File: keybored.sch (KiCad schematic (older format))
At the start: 24 parts, among them SW1 SW_Push, U1 ATmega32U4-AU, Y1 16MHz

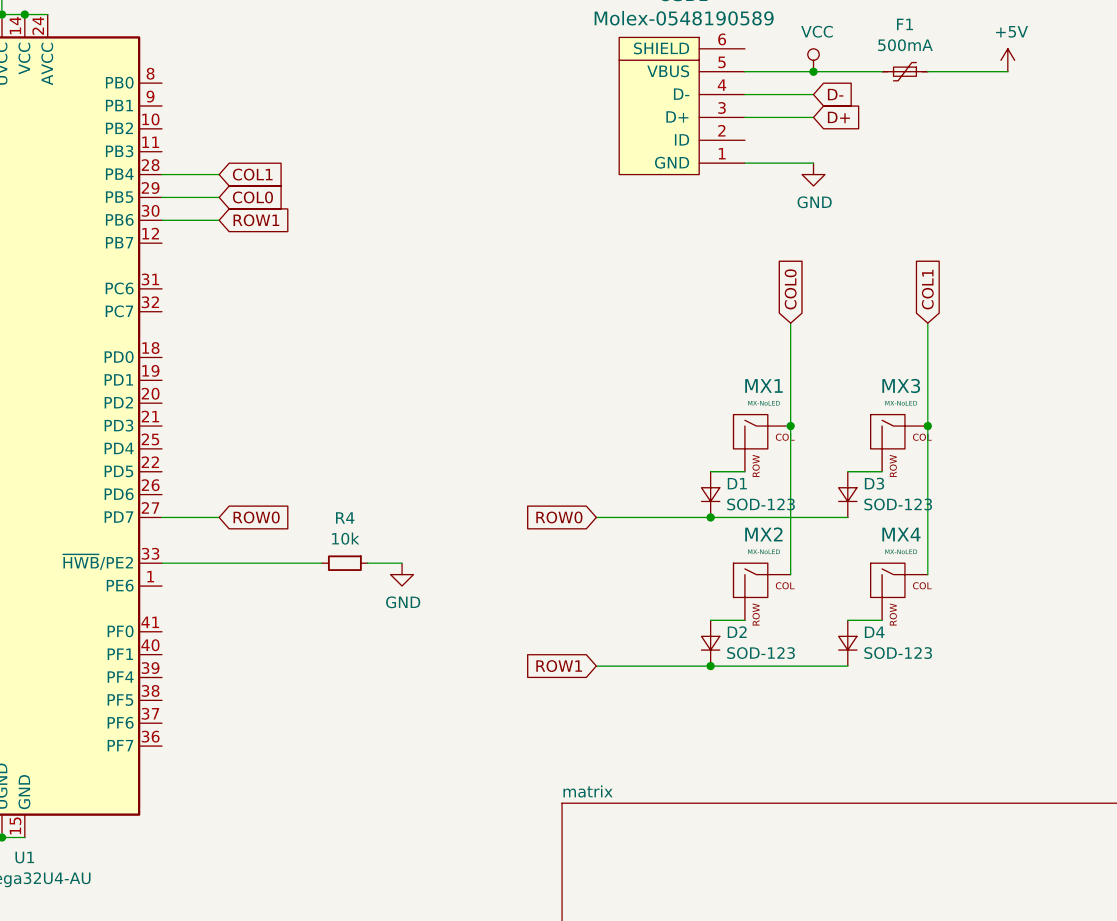
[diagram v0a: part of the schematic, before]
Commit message: updated main board schematic
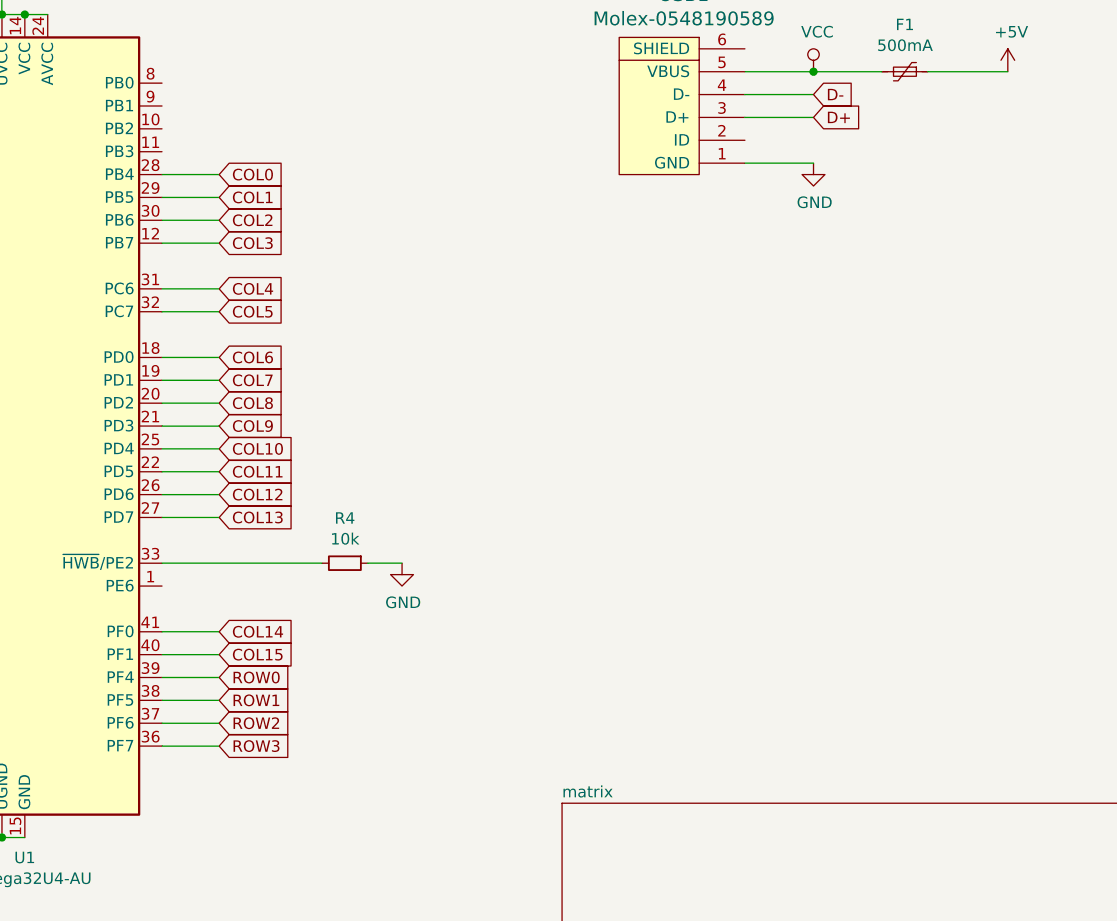
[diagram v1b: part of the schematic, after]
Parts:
- removed D1, D2, D3, D4: SOD-123, Diode_SMD:D_SOD-123, symbol Device:D_Small
- removed MX1, MX2, MX3, MX4: MX-NoLED, MX_Alps_Hybrid:MX-1U, symbol MX_Alps_Hybrid:MX-NoLED
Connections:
- net COL0: now also U1.28 (PB4); no longer U1.29 (PB5)
- net COL1: now also U1.29 (PB5); no longer U1.28 (PB4)
- net ROW0: now also U1.39 (PF4); no longer U1.27 (PD7)
- net ROW1: now also U1.38 (PF5); no longer U1.30 (PB6)
- net COL3: now reaches U1.12 (PB7)
- net COL6: now reaches U1.18 (PD0)
- net COL7: now reaches U1.19 (PD1)
- net COL8: now reaches U1.20 (PD2)
- net COL9: now reaches U1.21 (PD3)
- net COL11: now reaches U1.22 (PD5)
- net COL10: now reaches U1.25 (PD4)
- net COL12: now reaches U1.26 (PD6)
- net COL4: now reaches U1.31 (PC6)
- net COL5: now reaches U1.32 (PC7)
- net ROW3: now reaches U1.36 (PF7)
- net ROW2: now reaches U1.37 (PF6)
- net COL15: now reaches U1.40 (PF1)
- net COL14: now reaches U1.41 (PF0)
- new net COL13: U1.27 (PD7)
- new net COL2: U1.30 (PB6)
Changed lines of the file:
@@
 $Descr A4 11693 8268
 encoding utf-8
-Sheet 1 1
+Sheet 1 2
 Title ""
 Date ""
@@
 Wire Wire Line
 	7150 2150 6850 2150
-$Comp
-L MX_Alps_Hybrid:MX-NoLED MX1
-U 1 1 5F5BD9E0
-P 6900 3350
-F 0 "MX1" H 6933 3573 60  0000 C CNN
-F 1 "MX-NoLED" H 6933 3499 20  0000 C CNN
-F 2 "MX_Alps_Hybrid:MX-1U" H 6275 3325 60  0001 C CNN
-F 3 "" H 6275 3325 60  0001 C CNN
-	1    6900 3350
-	1    0    0    -1
-$EndComp
-Wire Wire Line
-	6700 3500 6850 3500
-$Comp
-L Device:D_Small D1
-U 1 1 5F5C01A3
-P 6700 3600
-F 0 "D1" V 6746 3532 50  0000 R CNN
-F 1 "SOD-123" V 6655 3532 50  0000 R CNN
-F 2 "Diode_SMD:D_SOD-123" V 6700 3600 50  0001 C CNN
-F 3 "~" V 6700 3600 50  0001 C CNN
-	1    6700 3600
-	0    -1   -1   0
-$EndComp
-$Comp
-L MX_Alps_Hybrid:MX-NoLED MX2
-U 1 1 5F5CC8AC
-P 6900 4000
-F 0 "MX2" H 6933 4223 60  0000 C CNN
-F 1 "MX-NoLED" H 6933 4149 20  0000 C CNN
-F 2 "MX_Alps_Hybrid:MX-1U" H 6275 3975 60  0001 C CNN
-F 3 "" H 6275 3975 60  0001 C CNN
-	1    6900 4000
-	1    0    0    -1
-$EndComp
-Wire Wire Line
-	6700 4150 6850 4150
-$Comp
-L Device:D_Small D2
-U 1 1 5F5CC8B3
-P 6700 4250
-F 0 "D2" V 6746 4182 50  0000 R CNN
-F 1 "SOD-123" V 6655 4182 50  0000 R CNN
-F 2 "Diode_SMD:D_SOD-123" V 6700 4250 50  0001 C CNN
-F 3 "~" V 6700 4250 50  0001 C CNN
-	1    6700 4250
-	0    -1   -1   0
-$EndComp
-$Comp
-L MX_Alps_Hybrid:MX-NoLED MX4
-U 1 1 5F5D07A5
-P 7500 4000
-F 0 "MX4" H 7533 4223 60  0000 C CNN
-F 1 "MX-NoLED" H 7533 4149 20  0000 C CNN
-F 2 "MX_Alps_Hybrid:MX-1U" H 6875 3975 60  0001 C CNN
-F 3 "" H 6875 3975 60  0001 C CNN
-	1    7500 4000
-	1    0    0    -1
-$EndComp
-Wire Wire Line
-	7300 4150 7450 4150
-$Comp
-L Device:D_Small D4
-U 1 1 5F5D07AC
-P 7300 4250
-F 0 "D4" V 7346 4182 50  0000 R CNN
-F 1 "SOD-123" V 7255 4182 50  0000 R CNN
-F 2 "Diode_SMD:D_SOD-123" V 7300 4250 50  0001 C CNN
-F 3 "~" V 7300 4250 50  0001 C CNN
-	1    7300 4250
-	0    -1   -1   0
-$EndComp
-$Comp
-L MX_Alps_Hybrid:MX-NoLED MX3
-U 1 1 5F5D2D0E
-P 7500 3350
-F 0 "MX3" H 7533 3573 60  0000 C CNN
-F 1 "MX-NoLED" H 7533 3499 20  0000 C CNN
-F 2 "MX_Alps_Hybrid:MX-1U" H 6875 3325 60  0001 C CNN
-F 3 "" H 6875 3325 60  0001 C CNN
-	1    7500 3350
-	1    0    0    -1
-$EndComp
-Wire Wire Line
-	7300 3500 7450 3500
-$Comp
-L Device:D_Small D3
-U 1 1 5F5D2D15
-P 7300 3600
-F 0 "D3" V 7346 3532 50  0000 R CNN
-F 1 "SOD-123" V 7255 3532 50  0000 R CNN
-F 2 "Diode_SMD:D_SOD-123" V 7300 3600 50  0001 C CNN
-F 3 "~" V 7300 3600 50  0001 C CNN
-	1    7300 3600
-	0    -1   -1   0
-$EndComp
-Wire Wire Line
-	7650 2850 7650 3300
-Connection ~ 7650 3300
-Wire Wire Line
-	7650 3300 7650 3950
-Wire Wire Line
-	7300 3700 6700 3700
-Connection ~ 6700 3700
-Wire Wire Line
-	6700 3700 6200 3700
-Wire Wire Line
-	7300 4350 6700 4350
-Connection ~ 6700 4350
-Wire Wire Line
-	6700 4350 6200 4350
-Wire Wire Line
-	7050 2850 7050 3300
-Connection ~ 7050 3300
-Wire Wire Line
-	7050 3300 7050 3950
-Text GLabel 6200 3700 0    50   Input ~ 0
-ROW0
-Text GLabel 6200 4350 0    50   Input ~ 0
-ROW1
-Text GLabel 7050 2850 1    50   Input ~ 0
+Text GLabel 4550 2200 2    50   Input ~ 0
 COL0
-Text GLabel 7650 2850 1    50   Input ~ 0
-COL1
-Text GLabel 4550 2200 2    50   Input ~ 0
-COL1
-Text GLabel 4550 2300 2    50   Input ~ 0
-COL0
-Text GLabel 4550 2400 2    50   Input ~ 0
-ROW1
-Text GLabel 4550 3700 2    50   Input ~ 0
-ROW0
-Wire Wire Line
-	4550 3700 4300 3700
-Wire Wire Line
-	4550 2400 4300 2400
 Wire Wire Line
 	4550 2300 4300 2300
@@
 F1 "matrix.sch" 50
 $EndSheet
+Text GLabel 4550 2300 2    50   Input ~ 0
+COL1
+Text GLabel 4550 2400 2    50   Input ~ 0
+COL2
+Text GLabel 4550 2500 2    50   Input ~ 0
+COL3
+Text GLabel 4550 2700 2    50   Input ~ 0
+COL4
+Text GLabel 4550 2800 2    50   Input ~ 0
+COL5
+Text GLabel 4550 3000 2    50   Input ~ 0
+COL6
+Text GLabel 4550 3100 2    50   Input ~ 0
+COL7
+Text GLabel 4550 3200 2    50   Input ~ 0
+COL8
+Text GLabel 4550 3300 2    50   Input ~ 0
+COL9
+Text GLabel 4550 3400 2    50   Input ~ 0
+COL10
+Text GLabel 4550 3500 2    50   Input ~ 0
+COL11
+Text GLabel 4550 3600 2    50   Input ~ 0
+COL12
+Text GLabel 4550 3700 2    50   Input ~ 0
+COL13
+Text GLabel 4550 4200 2    50   Input ~ 0
+COL14
+Text GLabel 4550 4300 2    50   Input ~ 0
+COL15
+Text GLabel 4550 4400 2    50   Input ~ 0
+ROW0
+Text GLabel 4550 4500 2    50   Input ~ 0
+ROW1
+Text GLabel 4550 4600 2    50   Input ~ 0
+ROW2
+Text GLabel 4550 4700 2    50   Input ~ 0
+ROW3
+Wire Wire Line
+	4550 2400 4300 2400
+Wire Wire Line
+	4300 2500 4550 2500
+Wire Wire Line
+	4550 2700 4300 2700
+Wire Wire Line
+	4550 2800 4300 2800
+Wire Wire Line
+	4300 3000 4550 3000
+Wire Wire Line
+	4550 3100 4300 3100
+Wire Wire Line
+	4300 3200 4550 3200
+Wire Wire Line
+	4550 3300 4300 3300
+Wire Wire Line
+	4300 3400 4550 3400
+Wire Wire Line
+	4550 3500 4300 3500
+Wire Wire Line
+	4300 3600 4550 3600
+Wire Wire Line
+	4550 3700 4300 3700
+Wire Wire Line
+	4300 4200 4550 4200
+Wire Wire Line
+	4550 4300 4300 4300
+Wire Wire Line
+	4300 4400 4550 4400
+Wire Wire Line
+	4550 4500 4300 4500
+Wire Wire Line
+	4300 4600 4550 4600
+Wire Wire Line
+	4550 4700 4300 4700
 $EndSCHEMATC

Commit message: I just wired up a 63-key board. yiiikes.
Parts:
- renumbered C3 to C_D0, C4 to C_D1, C5 to C_D2, C7 to C_D3, C6 to C_UCAP1, C1 to C_XTAL0, C2 to C_XTAL1, F1 to F_VBUS1, R3 to R_D+1, R1 to R_D-1, R4 to R_HWB1, R2 to R_RESET1, SW1 to SW_PUSH_RESET1
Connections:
- net COL0: now also U1.37 (PF6); no longer U1.28 (PB4)
- net COL1: now also U1.36 (PF7); no longer U1.29 (PB5)
- net COL10: now also U1.22 (PD5); no longer U1.25 (PD4)
- net COL11: now also U1.21 (PD3); no longer U1.22 (PD5)
- net COL12: now also U1.20 (PD2); no longer U1.26 (PD6)
- net COL13: now also U1.19 (PD1); no longer U1.27 (PD7)
- net COL14: now also U1.18 (PD0); no longer U1.41 (PF0)
- net COL15: now also U1.11 (PB3); no longer U1.40 (PF1)
- net COL2: now also U1.32 (PC7); no longer U1.30 (PB6)
- net COL3: now also U1.31 (PC6); no longer U1.12 (PB7)
- net COL4: now also U1.30 (PB6); no longer U1.31 (PC6)
- net COL5: now also U1.29 (PB5); no longer U1.32 (PC7)
- net COL6: now also U1.28 (PB4); no longer U1.18 (PD0)
- net COL7: now also U1.27 (PD7); no longer U1.19 (PD1)
- net COL8: now also U1.26 (PD6); no longer U1.20 (PD2)
- net COL9: now also U1.25 (PD4); no longer U1.21 (PD3)
- net ROW0: now also U1.38 (PF5); no longer U1.39 (PF4)
- net ROW1: now also U1.39 (PF4); no longer U1.38 (PF5)
- net ROW2: now also U1.40 (PF1); no longer U1.37 (PF6)
- net ROW3: now also U1.41 (PF0); no longer U1.36 (PF7)
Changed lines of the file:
@@
 Connection ~ 3600 5100
 $Comp
-L Device:R_Small R4
+L Device:R_Small R_HWB1
 U 1 1 5F57E4AB
 P 5100 3900
-F 0 "R4" V 4904 3900 50  0000 C CNN
+F 0 "R_HWB1" V 4904 3900 50  0000 C CNN
 F 1 "10k" V 4995 3900 50  0000 C CNN
 F 2 "Resistor_SMD:R_0805_2012Metric" H 5100 3900 50  0001 C CNN
@@
 	4300 3900 5000 3900
 $Comp
-L Device:R_Small R3
+L Device:R_Small R_D+1
 U 1 1 5F57FF45
 P 2800 2800
-F 0 "R3" V 2604 2800 50  0000 C CNN
+F 0 "R_D+1" V 2604 2800 50  0000 C CNN
 F 1 "22" V 2695 2800 50  0000 C CNN
 F 2 "Resistor_SMD:R_0805_2012Metric" H 2800 2800 50  0001 C CNN
@@
 $EndComp
 $Comp
-L Device:R_Small R1
+L Device:R_Small R_D-1
 U 1 1 5F5804A5
 P 2400 2900
-F 0 "R1" V 2204 2900 50  0000 C CNN
+F 0 "R_D-1" V 2204 2900 50  0000 C CNN
 F 1 "22" V 2295 2900 50  0000 C CNN
 F 2 "Resistor_SMD:R_0805_2012Metric" H 2400 2900 50  0001 C CNN
@@
 	3100 2900 2500 2900
 $Comp
-L Device:C_Small C6
+L Device:C_Small C_UCAP1
 U 1 1 5F58160B
 P 2600 3300
-F 0 "C6" H 2692 3346 50  0000 L CNN
+F 0 "C_UCAP1" H 2692 3346 50  0000 L CNN
 F 1 "1uF" H 2692 3255 50  0000 L CNN
 F 2 "Capacitor_SMD:C_0805_2012Metric" H 2600 3300 50  0001 C CNN
@@
 	2600 3450 2600 3400
 $Comp
-L Device:C_Small C3
+L Device:C_Small C_D0
 U 1 1 5F5835F2
 P 1900 4450
-F 0 "C3" H 1992 4496 50  0000 L CNN
+F 0 "C_D0" H 1992 4496 50  0000 L CNN
 F 1 "0.1uF" H 1992 4405 50  0000 L CNN
 F 2 "Capacitor_SMD:C_0805_2012Metric" H 1900 4450 50  0001 C CNN
@@
 $EndComp
 $Comp
-L Device:C_Small C4
+L Device:C_Small C_D1
 U 1 1 5F5842E1
 P 2150 4450
-F 0 "C4" H 2242 4496 50  0000 L CNN
+F 0 "C_D1" H 2242 4496 50  0000 L CNN
 F 1 "0.1uF" H 2242 4405 50  0000 L CNN
 F 2 "Capacitor_SMD:C_0805_2012Metric" H 2150 4450 50  0001 C CNN
@@
 $EndComp
 $Comp
-L Device:C_Small C5
+L Device:C_Small C_D2
 U 1 1 5F5846CF
 P 2450 4450
-F 0 "C5" H 2542 4496 50  0000 L CNN
+F 0 "C_D2" H 2542 4496 50  0000 L CNN
 F 1 "0.1uF" H 2542 4405 50  0000 L CNN
 F 2 "Capacitor_SMD:C_0805_2012Metric" H 2450 4450 50  0001 C CNN
@@
 $EndComp
 $Comp
-L Device:C_Small C7
+L Device:C_Small C_D3
 U 1 1 5F584C7C
 P 2700 4450
-F 0 "C7" H 2792 4496 50  0000 L CNN
+F 0 "C_D3" H 2792 4496 50  0000 L CNN
 F 1 "10uF" H 2792 4405 50  0000 L CNN
 F 2 "Capacitor_SMD:C_0805_2012Metric" H 2700 4450 50  0001 C CNN
@@
 	2250 2200 3100 2200
 $Comp
-L Device:C_Small C1
+L Device:C_Small C_XTAL0
 U 1 1 5F59337E
 P 1850 1850
-F 0 "C1" V 2079 1850 50  0000 C CNN
+F 0 "C_XTAL0" V 2079 1850 50  0000 C CNN
 F 1 "22pF" V 1988 1850 50  0000 C CNN
 F 2 "Capacitor_SMD:C_0805_2012Metric" H 1850 1850 50  0001 C CNN
@@
 $EndComp
 $Comp
-L Device:C_Small C2
+L Device:C_Small C_XTAL1
 U 1 1 5F59434C
 P 1850 2300
-F 0 "C2" V 1621 2300 50  0000 C CNN
+F 0 "C_XTAL1" V 1621 2300 50  0000 C CNN
 F 1 "22pF" V 1712 2300 50  0000 C CNN
 F 2 "Capacitor_SMD:C_0805_2012Metric" H 1850 2300 50  0001 C CNN
@@
 Connection ~ 1600 2500
 $Comp
-L Switch:SW_Push SW1
+L Switch:SW_Push SW_PUSH_RESET1
 U 1 1 5F5993F7
 P 2450 1800
-F 0 "SW1" H 2450 2085 50  0000 C CNN
+F 0 "SW_PUSH_RESET1" H 2450 2085 50  0000 C CNN
 F 1 "SW_Push" H 2450 1994 50  0000 C CNN
 F 2 "random-keyboard-parts:SKQG-1155865" H 2450 2000 50  0001 C CNN
@@
 	2250 1750 2250 1800
 $Comp
-L Device:R_Small R2
+L Device:R_Small R_RESET1
 U 1 1 5F59BDA9
 P 2750 1600
-F 0 "R2" H 2809 1646 50  0000 L CNN
+F 0 "R_RESET1" H 2809 1646 50  0000 L CNN
 F 1 "10k" H 2809 1555 50  0000 L CNN
 F 2 "Resistor_SMD:R_0805_2012Metric" H 2750 1600 50  0001 C CNN
@@
 $EndComp
 $Comp
-L Device:Polyfuse_Small F1
+L Device:Polyfuse_Small F_VBUS1
 U 1 1 5F5B277E
 P 7550 1750
-F 0 "F1" V 7345 1750 50  0000 C CNN
+F 0 "F_VBUS1" V 7345 1750 50  0000 C CNN
 F 1 "500mA" V 7436 1750 50  0000 C CNN
 F 2 "Fuse:Fuse_1206_3216Metric" H 7600 1550 50  0001 L CNN
@@
 $EndComp
 $Comp
-L power:VCC #PWR0111
+L power:VCC #VCC_VBUS0101
 U 1 1 5F5B38E9
 P 7150 1750
-F 0 "#PWR0111" H 7150 1600 50  0001 C CNN
+F 0 "#VCC_VBUS0101" H 7150 1600 50  0001 C CNN
 F 1 "VCC" H 7167 1923 50  0000 C CNN
 F 2 "" H 7150 1750 50  0001 C CNN
@@
 	7150 2150 6850 2150
 Text GLabel 4550 2200 2    50   Input ~ 0
-COL0
+COL6
 Wire Wire Line
 	4550 2300 4300 2300
@@
 $EndSheet
 Text GLabel 4550 2300 2    50   Input ~ 0
-COL1
+COL5
 Text GLabel 4550 2400 2    50   Input ~ 0
+COL4
+Text GLabel 4550 2700 2    50   Input ~ 0
+COL3
+Text GLabel 4550 2800 2    50   Input ~ 0
 COL2
-Text GLabel 4550 2500 2    50   Input ~ 0
-COL3
-Text GLabel 4550 2700 2    50   Input ~ 0
-COL4
-Text GLabel 4550 2800 2    50   Input ~ 0
-COL5
 Text GLabel 4550 3000 2    50   Input ~ 0
-COL6
+COL14
 Text GLabel 4550 3100 2    50   Input ~ 0
+COL13
+Text GLabel 4550 3200 2    50   Input ~ 0
+COL12
+Text GLabel 4550 3300 2    50   Input ~ 0
+COL11
+Text GLabel 4550 3400 2    50   Input ~ 0
+COL9
+Text GLabel 4550 3500 2    50   Input ~ 0
+COL10
+Text GLabel 4550 3600 2    50   Input ~ 0
+COL8
+Text GLabel 4550 3700 2    50   Input ~ 0
 COL7
-Text GLabel 4550 3200 2    50   Input ~ 0
-COL8
-Text GLabel 4550 3300 2    50   Input ~ 0
-COL9
-Text GLabel 4550 3400 2    50   Input ~ 0
-COL10
-Text GLabel 4550 3500 2    50   Input ~ 0
-COL11
-Text GLabel 4550 3600 2    50   Input ~ 0
-COL12
-Text GLabel 4550 3700 2    50   Input ~ 0
-COL13
 Text GLabel 4550 4200 2    50   Input ~ 0
-COL14
+ROW3
 Text GLabel 4550 4300 2    50   Input ~ 0
-COL15
+ROW2
 Text GLabel 4550 4400 2    50   Input ~ 0
-ROW0
-Text GLabel 4550 4500 2    50   Input ~ 0
 ROW1
 Text GLabel 4550 4600 2    50   Input ~ 0
-ROW2
+COL0
 Text GLabel 4550 4700 2    50   Input ~ 0
-ROW3
+COL1
 Wire Wire Line
 	4550 2400 4300 2400
 Wire Wire Line
-	4300 2500 4550 2500
-Wire Wire Line
 	4550 2700 4300 2700
 Wire Wire Line
@@
 Wire Wire Line
 	4550 4700 4300 4700
+Text GLabel 4550 4500 2    50   Input ~ 0
+ROW0
+Text GLabel 4550 2100 2    50   Input ~ 0
+COL15
+Wire Wire Line
+	4550 2100 4300 2100
 $EndSCHEMATC
